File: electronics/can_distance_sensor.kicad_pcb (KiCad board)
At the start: 4 copper layers, 39.4 x 47.6 mm, 81 parts, among them J1 USB_B_Micro, J2 Conn_ARM_JTAG_SWD_10, J4 Conn_01x02_Socket, J5 Conn_01x04, Q1 IRLML6401, SW1 PTS645SK50SMTR92LFS, U1 USBLC6-2SC6, U2 STM32F446RETx, U3 LM1117DT-ADJ, U4 AOZ1280CI, U6 TCAN1043xDxQ1, U7 VL53L5CXV0GC/1, Y1 Crystal_GND24

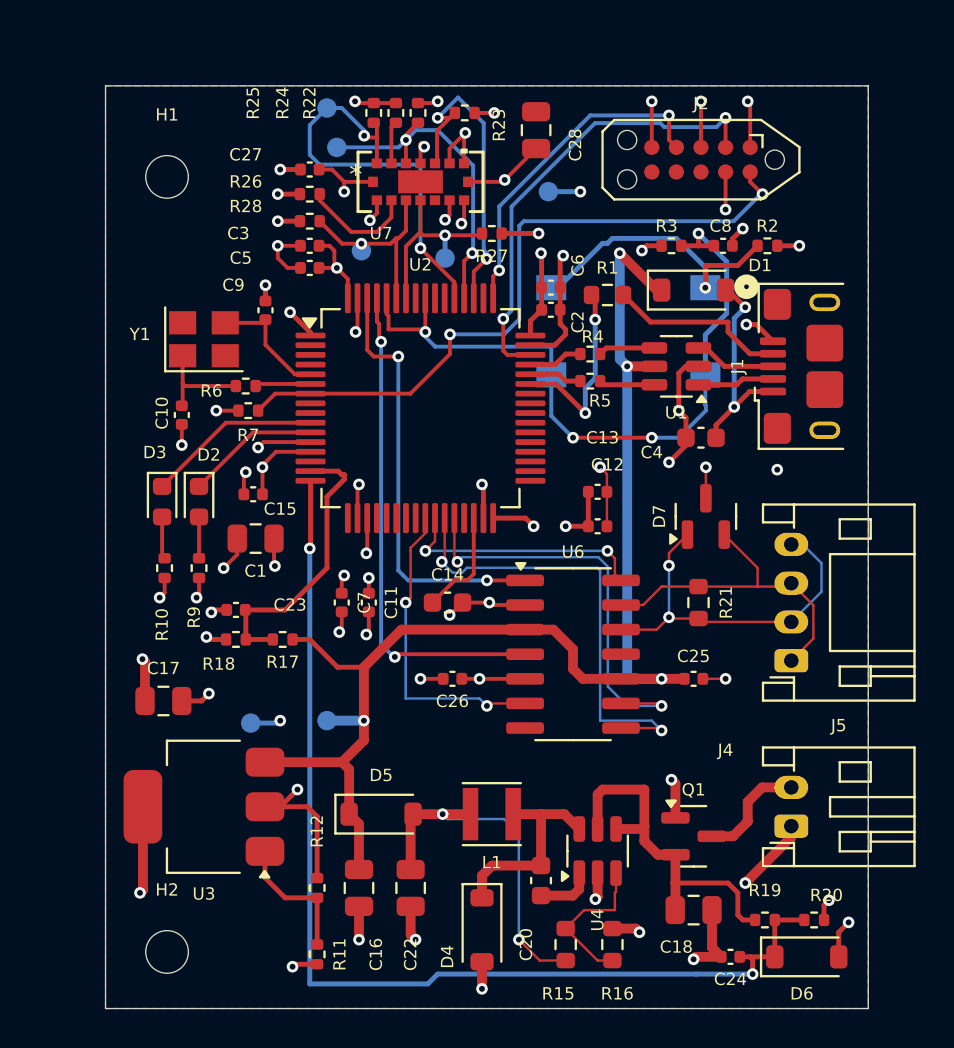
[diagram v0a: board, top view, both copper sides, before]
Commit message: Switched to a lower cost TOF sensor.
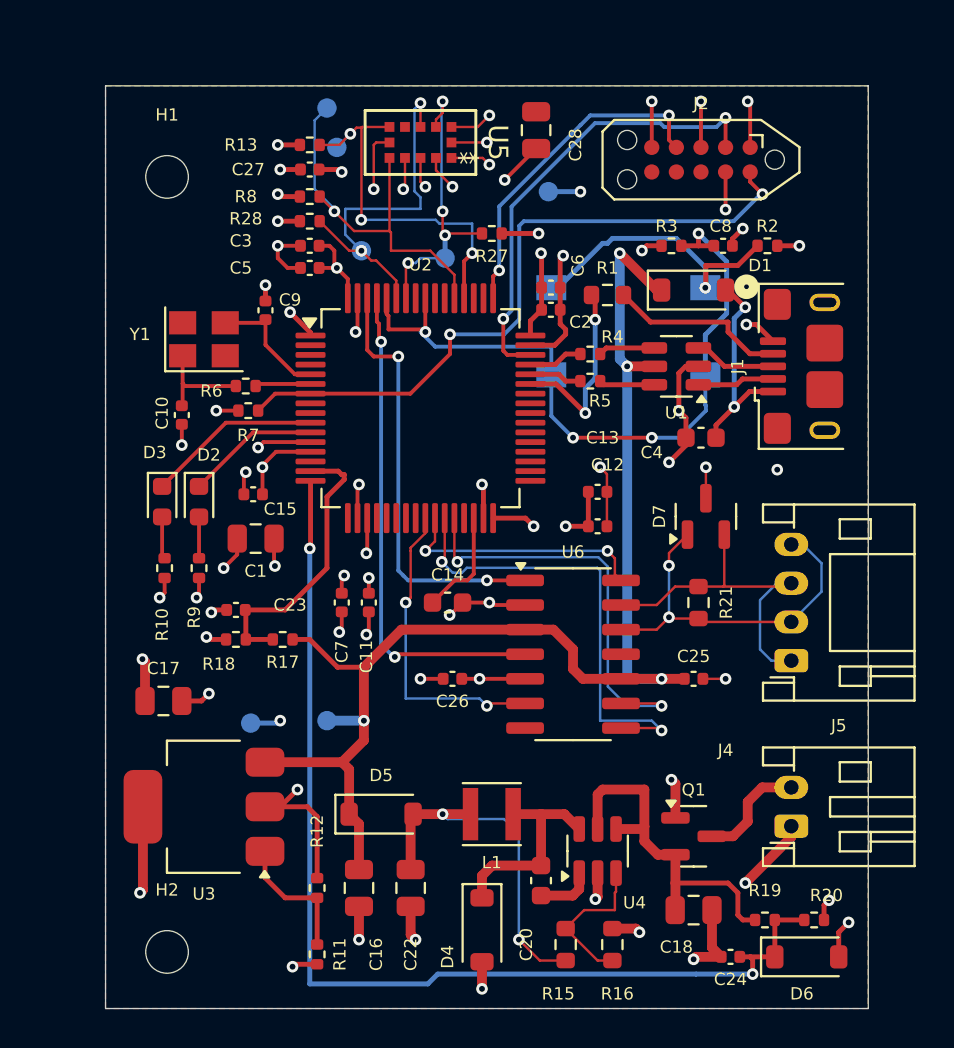
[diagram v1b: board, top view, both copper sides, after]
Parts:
- removed R22, R23, R25, R26: 47k, Resistor_SMD:R_0402_1005Metric
- removed R24: 0, Resistor_SMD:R_0402_1005Metric
- removed U7: VL53L5CXV0GC/1, footprints:LGA_CXV0GC
- added R13: 10K, Resistor_SMD:R_0402_1005Metric, F.Cu at (187.7, 90.8)
- added R8: 10K, Resistor_SMD:R_0402_1005Metric, F.Cu at (187.7, 93.5)
- added U5: VL53L3CXV0DH/1, footprints:LGA12_STM, F.Cu at (193.4, 90.7)
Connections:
- net TOF_RST renamed TOF_XSHUT
- U2 pad 51: TOF_LP -> unconnected-(U2-PC10-Pad51)
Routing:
- net TOF_LP: track 16.8 -> 0.00 mm, vias 2 -> 0
- net TOF_SDA: track 10.2 -> 19.5 mm, vias 1 -> 2
- net Net-(U7-GPIO2): track 5.90 -> 0.00 mm
- net TOF_SCL: track 9.85 -> 15.5 mm, vias 1 -> 4
- net Net-(U7-NCS): track 2.19 -> 0.00 mm
- net TOF_INT: track 17.6 -> 19.6 mm, vias 2 -> 3
- net 3V3: track 66.9 -> 65.1 mm
- net TOF_XSHUT: track 21.9 -> 20.2 mm, vias 2 -> 1
- net GND: track 90.8 -> 91.6 mm
- net Net-(J5-Pin_1): track 17.7 -> 18.3 mm

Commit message: Ordered this version.
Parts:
- removed C11, C12, C13: 0.1u, Capacitor_SMD:C_0402_1005Metric
- removed C14: 2.2u, Capacitor_SMD:C_0603_1608Metric
- removed the C16 at (190.2, 129.2)
- removed the C23 at (183.9, 114.8)
- removed H1, H2: MountingHole, MountingHole:MountingHole_2.2mm_M2
- removed J4: Conn_01x02_Socket, Connector_JST:JST_PH_S2B-PH-K_1x02_P2.00mm_Horizontal
- removed the R12 at (188.1, 129.2)
- removed the R17 at (186.3, 116.3)
- removed the R18 at (183.9, 116.3)
- added C27: 4.7u, Capacitor_SMD:C_0603_1608Metric, F.Cu at (188.7, 114.4)
- added C28: 4.7u, Capacitor_SMD:C_0603_1608Metric, F.Cu at (181.4, 114.4)
- added R10: 5k, Resistor_SMD:R_0402_1005Metric, F.Cu at (183.1, 113.2)
- added R14: 4.09k, Resistor_SMD:R_0402_1005Metric, F.Cu at (185.4, 118.4)
- added R15: 1k, Resistor_SMD:R_0402_1005Metric, F.Cu at (185.4, 120.7)
- added R22: 10K, Resistor_SMD:R_0402_1005Metric, F.Cu at (197.6, 102.4)
- added TP8: TestPoint, TestPoint:TestPoint_Pad_D1.0mm, B.Cu at (180.3, 117.9)
- added U5: TLV75801PDRV, Package_SON:WSON-6-1EP_2x2mm_P0.65mm_EP1x1.6mm, F.Cu at (188.2, 119.4)
- added U8: TCA9509DGKR, footprints:DGK8, F.Cu at (192.0, 101.6)
- C1: footprint Capacitor_SMD:C_0805_2012Metric -> Capacitor_SMD:C_0603_1608Metric
- C15: value 0.1u -> 4.7u; footprint Capacitor_SMD:C_0402_1005Metric -> Capacitor_SMD:C_0603_1608Metric
- C16: renamed from C18; footprint Capacitor_SMD:C_0805_2012Metric -> Capacitor_SMD:C_0603_1608Metric
- C17: value 10u -> 4.7u; footprint Capacitor_SMD:C_0805_2012Metric -> Capacitor_SMD:C_0603_1608Metric
- C20: renamed from C22; footprint Capacitor_SMD:C_0805_2012Metric -> Capacitor_SMD:C_0603_1608Metric
- C26: renamed from C28; footprint Capacitor_SMD:C_0805_2012Metric -> Capacitor_SMD:C_0603_1608Metric
- J2: moved to B.Cu
- L1: footprint Inductor_SMD:L_Taiyo-Yuden_MD-3030 -> Inductor_SMD:L_1210_3225Metric
- R1: footprint Resistor_SMD:R_0603_1608Metric -> Resistor_SMD:R_0402_1005Metric
- R11: value 1.6k -> 1k
- R12: renamed from R15; footprint Resistor_SMD:R_0603_1608Metric -> Resistor_SMD:R_0402_1005Metric
- R13: renamed from R16; footprint Resistor_SMD:R_0603_1608Metric -> Resistor_SMD:R_0402_1005Metric
- R18: renamed from R21; footprint Resistor_SMD:R_0603_1608Metric -> Resistor_SMD:R_0402_1005Metric
- U2: value STM32F446RETx -> STM32G431CBUx; footprint Package_QFP:LQFP-64_10x10mm_P0.5mm -> Package_DFN_QFN:QFN-48-1EP_7x7mm_P0.5mm_EP5.6x5.6mm
- U3: value LM1117DT-ADJ -> TLV75801PDRV; footprint Package_TO_SOT_SMD:SOT-223-3_TabPin2 -> Package_SON:WSON-6-1EP_2x2mm_P0.65mm_EP1x1.6mm
- U6: value TCAN1043xDxQ1 -> TCAN1044A-Q1; footprint Package_SO:SOIC-14_3.9x8.7mm_P1.27mm -> Package_SON:VSON-8-1EP_3x3mm_P0.65mm_EP1.6x2.4mm
- moved J1 38.7 mm to (175.8, 105.7), turned to -90 degrees
- moved R9 32.2 mm to (201.3, 88.3)
- moved C4 32.1 mm to (176.5, 99.1), turned to 90 degrees
- moved R8 29.4 mm to (196.3, 87.0)
- moved D3 28.9 mm to (199.6, 88.0), turned to 90 degrees
- moved D1 28.7 mm to (178.8, 98.0), turned to 90 degrees
- moved C7 27.4 mm to (191.3, 87.1), turned to 90 degrees
- moved D2 26.9 mm to (198.0, 87.6), turned to 90 degrees
- moved C1 26.0 mm to (194.8, 87.1), turned to 90 degrees
- moved C10 25.5 mm to (201.9, 90.0), turned to 180 degrees
- moved J2 25.0 mm to (183.1, 95.2), turned to 90 degrees
- moved U1 24.0 mm to (182.9, 105.7), turned to 0 degrees
- moved R1 23.9 mm to (181.6, 109.0), turned to 180 degrees
- moved Y1 21.5 mm to (202.3, 93.2), turned to -90 degrees
- moved D6 19.9 mm to (195.8, 123.2), turned to 180 degrees
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- renumbered C20 to C18, C24 to C22, C25 to C23, C26 to C24, C27 to C25, J5 to J3, R19 to R16, R20 to R17, R8 to R19, R13 to R20, R27 to R21, R28 to R23, R9 to R8, R10 to R9, TP2 to TP1, TP4 to TP2, TP5 to TP3, TP6 to TP4, TP7 to TP5, TP1 to TP6, TP3 to TP7, U5 to U7
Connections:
- net Net-(D4-K) renamed /Power/LX
- net Net-(D5-A) renamed /Power/PRE_OUT
- C15 pad 1: 3V3 -> VCC
- C17 pad 1: 3V3 -> 2V8
- C25 pad 1: 3V3 -> 2V8
- C26 pad 1: 3V3 -> 2V8
- D7 pad 1: Net-(J5-Pin_2) -> Net-(J3-Pin_3)
- D7 pad 2: Net-(J5-Pin_1) -> Net-(J3-Pin_4)
- J3 pad 1: Net-(J5-Pin_1) -> VIN
- J3 pad 2: Net-(J5-Pin_2) -> GND
- J3 pad 3: Net-(J5-Pin_1) -> Net-(J3-Pin_3)
- J3 pad 4: Net-(J5-Pin_2) -> Net-(J3-Pin_4)
- Q1 pad 3: /Power/VIN -> VIN
- R11 pad 1: Net-(U3-ADJ) -> Net-(U3-FB)
- R18 pad 1: Net-(J5-Pin_1) -> Net-(J3-Pin_4)
- R18 pad 2: Net-(J5-Pin_2) -> Net-(J3-Pin_3)
- R19 pad 1: 3V3 -> 2V8
- R20 pad 1: 3V3 -> 2V8
- R21 pad 1: 3V3 -> 2V8
- R21 pad 2: TOF_SCL -> TOF_SCL_2V8
- R23 pad 1: 3V3 -> 2V8
- R23 pad 2: TOF_SDA -> TOF_SDA_2V8
- U2 pad 10: LED2 -> unconnected-(U2-PA2-Pad10)
- U2 pad 11: LED1 -> unconnected-(U2-PA3-Pad11)
- U2 pad 12: GND -> unconnected-(U2-PA4-Pad12)
- U2 pad 13: 3V3 -> BOOT
- U2 pad 14: ANALOG_IN -> LED2
- U2 pad 15: VCC_MEAS -> LED1
- U2 pad 16: VIN_MEAS -> unconnected-(U2-PC4-Pad16)
- U2 pad 18: GND -> unconnected-(U2-PB1-Pad18)
- U2 pad 19: 3V3 -> unconnected-(U2-PB2-Pad19)
- U2 pad 2: unconnected-(U2-PC13-Pad2) -> CAN_STB
- U2 pad 20: unconnected-(U2-PA4-Pad20) -> 3V3
- U2 pad 21: unconnected-(U2-PA5-Pad21) -> 3V3
- U2 pad 23: unconnected-(U2-PA7-Pad23) -> 3V3
- U2 pad 25: CAN_EN -> unconnected-(U2-PB12-Pad25)
- U2 pad 26: CAN_STB -> unconnected-(U2-PB13-Pad26)
- U2 pad 27: CAN_FAULT -> unconnected-(U2-PB14-Pad27)
- U2 pad 28: CAN_WAKE -> unconnected-(U2-PB15-Pad28)
- U2 pad 30: Net-(U2-VCAP_1) -> unconnected-(U2-PA8-Pad30)
- U2 pad 31: GND -> unconnected-(U2-PA9-Pad31)
- U2 pad 32: 3V3 -> ID
- U2 pad 33: unconnected-(U2-PB12-Pad33) -> DM
- U2 pad 34: unconnected-(U2-PB13-Pad34) -> DP
- U2 pad 35: unconnected-(U2-PB14-Pad35) -> 3V3
- U2 pad 36: unconnected-(U2-PB15-Pad36) -> SWDIO
- U2 pad 37: unconnected-(U2-PC6-Pad37) -> SWCLK
- U2 pad 38: unconnected-(U2-PC7-Pad38) -> TOF_SCL
- U2 pad 43: ID -> TOF_INT
- U2 pad 44: DM -> TOF_XSHUT
- U2 pad 45: DP -> TOF_SDA
- U2 pad 46: SWDIO -> CAN_RX
- U2 pad 47: GND -> CAN_TX
- U2 pad 49: SWCLK -> GND
- U2 pad 8: unconnected-(U2-PC0-Pad8) -> VIN_MEAS
- U3 pad 1: Net-(U3-ADJ) -> 3V3
- U3 pad 2: 3V3 -> Net-(U3-FB)
- U3 pad 3: VCC -> GND
- U6 pad 6: CAN_EN -> Net-(J3-Pin_3)
- U6 pad 7: unconnected-(U6-INH-Pad7) -> Net-(J3-Pin_4)
- U6 pad 8: CAN_FAULT -> CAN_STB
- U6 pad 9: CAN_WAKE -> (no net)
- U7 pad 1: 3V3 -> 2V8
- U7 pad 10: TOF_SCL -> TOF_SCL_2V8
- U7 pad 11: 3V3 -> 2V8
- U7 pad 9: TOF_SDA -> TOF_SDA_2V8
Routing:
- net 2V8: track 0.00 -> 61.0 mm, vias 0 -> 2
- net GND: track 91.6 -> 49.1 mm, vias 48 -> 33
- net 3V3: track 65.1 -> 36.2 mm, vias 28 -> 17
- net CAN_FAULT: track 24.2 -> 0.00 mm, vias 2 -> 0
- net CAN_WAKE: track 21.9 -> 0.00 mm, vias 2 -> 0
- net Net-(J5-Pin_2): track 19.5 -> 0.00 mm, vias 2 -> 0
- net ID: track 9.84 -> 28.9 mm
- net Net-(J5-Pin_1): track 18.3 -> 0.00 mm
- net Net-(J3-Pin_4): track 0.00 -> 16.4 mm
- net CAN_EN: track 16.1 -> 0.00 mm, vias 2 -> 0
- net VCC_MEAS: track 15.0 -> 0.00 mm
- net CAN_TX: track 22.2 -> 8.67 mm, vias 2 -> 0
- net CAN_RX: track 25.7 -> 12.7 mm
- net NRST: track 35.5 -> 23.9 mm
- net /Power/LX: track 10.8 -> 0.00 mm
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- added copper zone on F.Cu, net /Power/LX
- added copper zone on F.Cu, net /Power/PRE_OUT
- added copper zone on B.Cu, net GND
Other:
- board size 39.4 x 47.6 mm -> 40.6 x 40.6 mm
- board text added: "TP1 = 3.3V TP2 = TOF_SDA TP3 = VCC TP4 = TOF_SCL TP5 = TOF_INT TP6 = TOF_XSHUT TP7 = GND"
- board text removed: "TP1 = 3.3V TP2 = TOF_SDA TP3 = VCC TP4 = TOF_SCL TP5 = TOF_INT TP6 = TOF_RST TP7 = GND"
